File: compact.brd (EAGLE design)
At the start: 21.6 x 57.1 mm, 39 parts, among them J3 AVX_6-PIN_009159006061916, J4 CORTEX_DEBUG_PTH, J5 2172034-1, U1 STM32F103C8T6, U2 CJT1117-3.3-SOT223

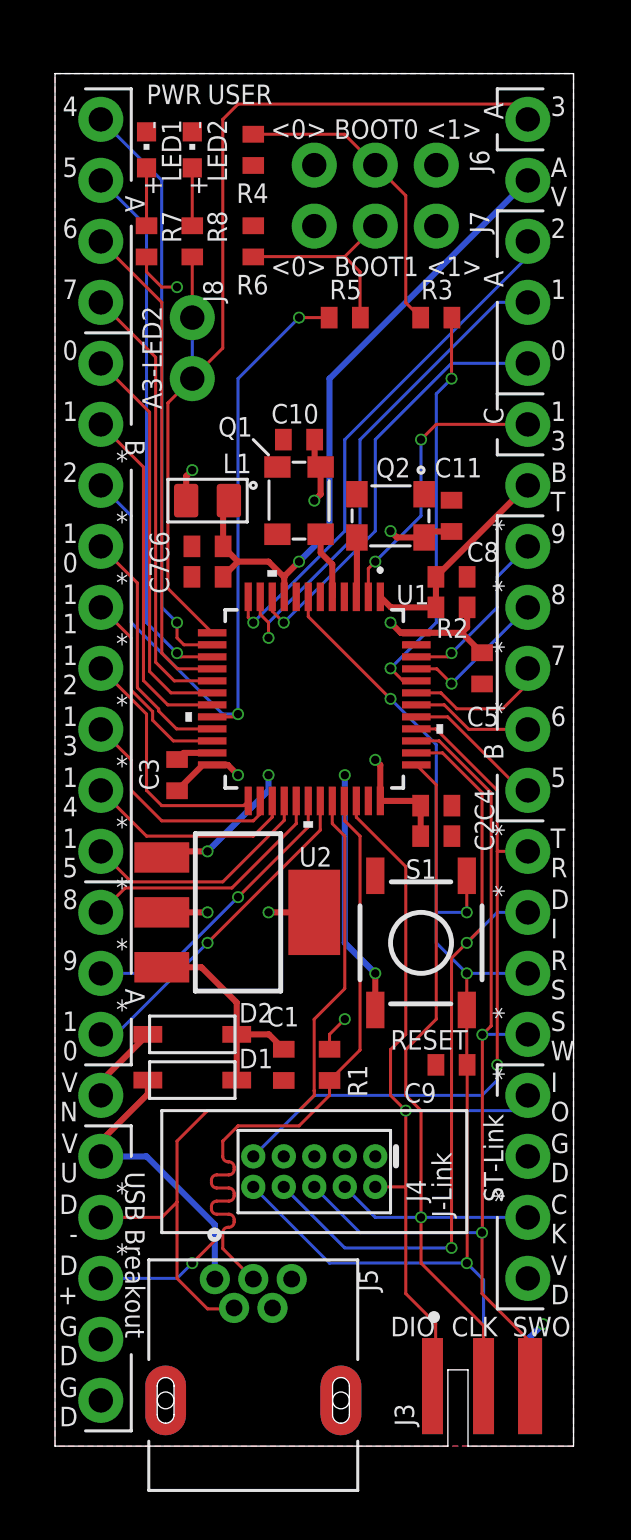
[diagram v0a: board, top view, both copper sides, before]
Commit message: Separated Standard configuration into Standard-no-HSE and Standard-with-HSE configurations.
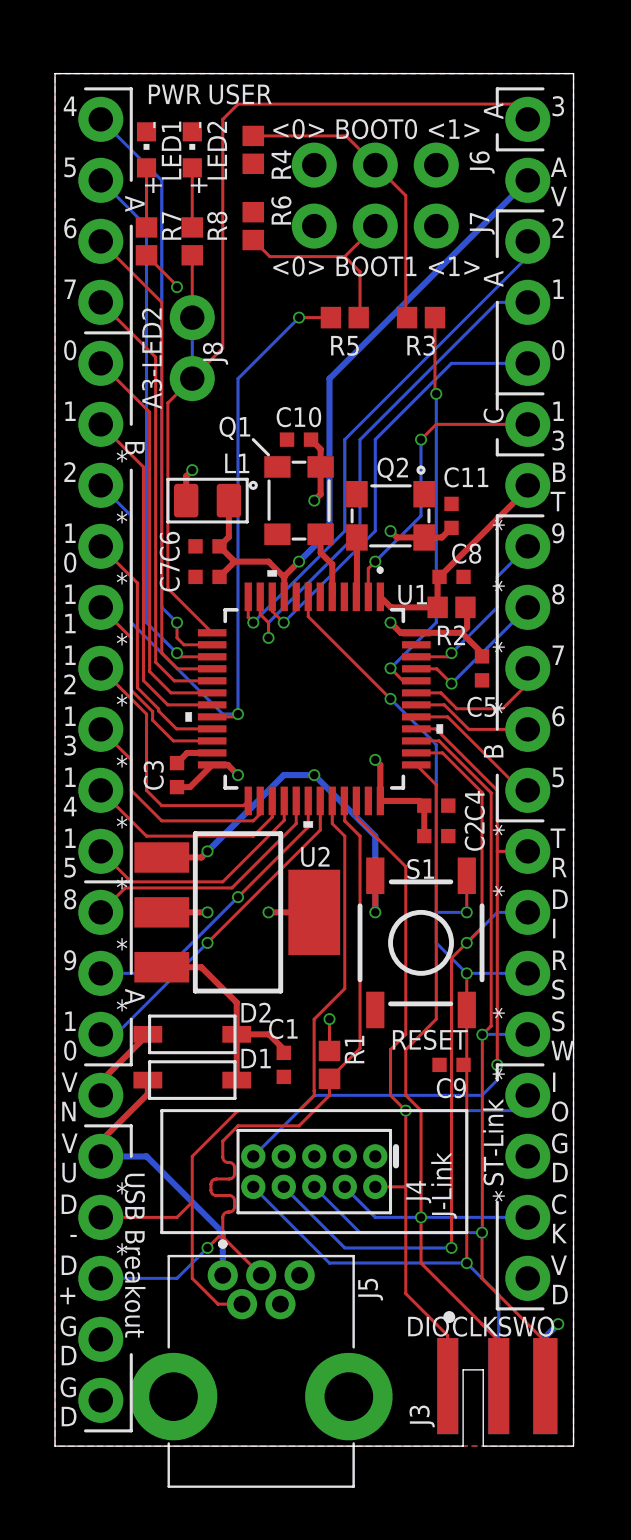
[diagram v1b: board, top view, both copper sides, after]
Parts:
- C1, C10, C11, C2, C3, C4, C5, C6, C7, C8, C9: device adafruit:C0402 -> SparkFun-Capacitors:0402-TIGHT
- J5: device USB-mini-B_TE_2172034-1:TE_2172034-1 -> 2172034-1:21720341
- R1, R2, R3, R4, R5, R6, R7, R8: device adafruit:R0402 -> SparkFun-Resistors:0402
- moved J5 5.36 mm to (6.99, 7.11)
- moved R3 0.63 mm to (15.2, 47.0)
- moved J3 0.63 mm to (18.4, 0.00)
- moved R6 0.63 mm to (8.26, 50.8)
- turned R8 to 270 degrees
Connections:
- net GND: now also J5.MH1, J5.MH2; no longer J5.SH1, J5.SH2
- net N$4: now also R8.1; no longer R8.2
- net PA3: now also R8.2; no longer R8.1
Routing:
- net USB_DP*: track 33.6 -> 32.3 mm
- net USB_DM*: track 31.6 -> 30.8 mm
- net GND: track 20.9 -> 20.5 mm, vias 5 -> 4
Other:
- outline, holes or cut-outs redrawn
- board text added: "-------POWER------- VDD/AVDD: 2-3.6V. Must be 3.3V if C39- 097/C387- 415 are used for Q1/Q2. VUSB: 5V from USB (J5) VIN: 4.8-15V BAT: 1.8-3.6V. Short R2 if unused. ***WARNING***: Do NOT power MCU from VDD if EITHER VIN or USB (J5) are also being used. --------GPIO-------- Max current, ea pin: 25 mA Max current, total: 150 mA OUT (minus MCU power, ~7 -50 mA) and 150 mA IN (minus MCU power) *=5V to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"
- board text added: "GD"
- board text removed: "-------POWER------- VDD/AVDD: 2-3.6V. Must be 3.3V if C39- 097/C387- 415 are used for Q1/Q2. VUSB: 5V from USB (J5) VIN: 4.8-15V BAT: 1.8-3.6V. Short R2 if unused. ***WARNING***: Do NOT power MCU from VDD if EITHER VIN or USB (J5) are also being used. --------GPIO-------- Max current, ea pin: 25 mA Max current, total: 150 mA OUT (minus MCU power, ~7 -50 mA) and 150 mA IN (minus MCU po- wer) *=5V 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"
- board text removed: "GND"

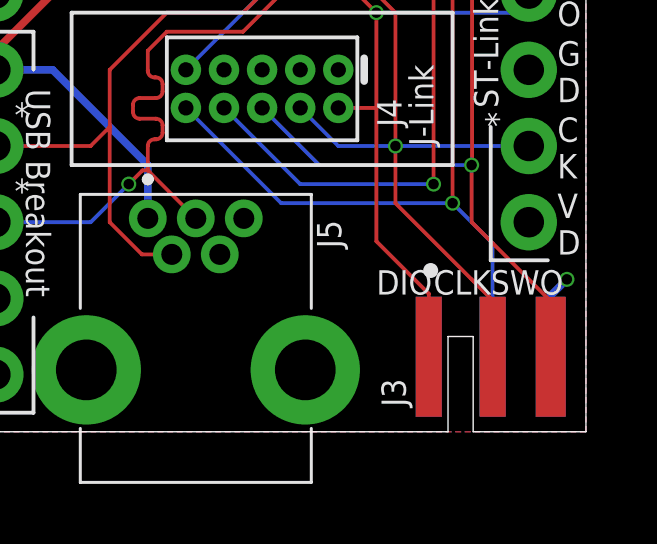
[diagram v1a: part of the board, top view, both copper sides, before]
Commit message: Updated Debug Edge library. Updated Gerbers, screenshots, and schematic image. Switched to new Mini-B USB footprint.
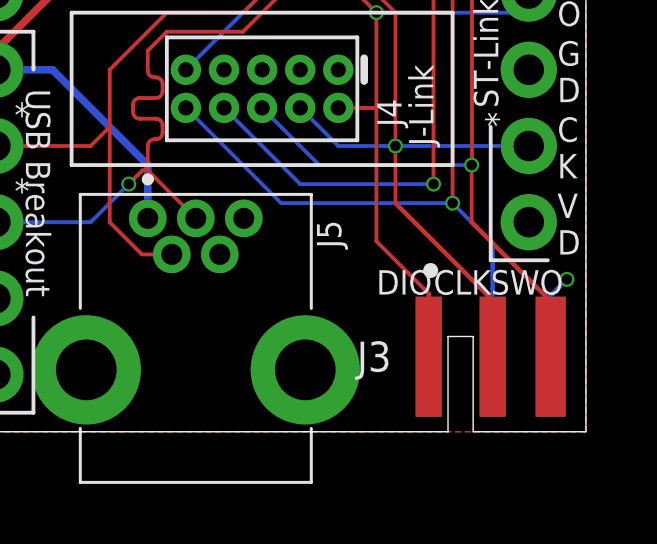
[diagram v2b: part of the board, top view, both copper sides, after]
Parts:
- J3: value AVX_6-PIN_009159006061916 -> AVX_6-PIN_009159006061916_33MIL-GAP; device Debug-Edge_AVX-connectors:AVX_6-PIN_009159006061916_0 -> Debug-Edge_AVX-connectors:AVX_6-PIN_009159006061916_33MIL-GAP
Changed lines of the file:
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@@
 <attribute name="VALUE" x="7.747" y="43.18" size="0.6096" layer="27" font="vector" ratio="20" rot="R90"/>
-</element>
-<element name="J3" library="Debug-Edge_AVX-connectors" package="AVX_6-PIN_009159006061916_0" value="AVX_6-PIN_009159006061916" x="18.415" y="0" smashed="yes">
-<attribute name="NAME" x="14.775" y="1.77" size="0.8128" layer="25" ratio="6" rot="R270"/>
 </element>
 <element name="L1" library="OPL_Ferrite_and_Magnetic_Bead" package="L0805" package3d_urn="urn:adsk.eagle:package:8004624/1" value="470R-2A" x="6.35" y="39.37" smashed="yes" rot="R180">
@@
 <attribute name="VALUE" x="8.585" y="3.412" size="1.27" layer="27" rot="R270" align="center"/>
 </element>
+<element name="J3" library="Debug-Edge_AVX-connectors" package="AVX_6-PIN_009159006061916_33MIL-GAP" value="AVX_6-PIN_009159006061916_33MIL-GAP" x="18.415" y="0" smashed="yes">
+<attribute name="NAME" x="15.105" y="3.005" size="1" layer="25" rot="R180"/>
+</element>
 </elements>
 <signals>
@@
 <contactref element="U1" pad="7"/>
 <contactref element="J4" pad="10"/>
-<contactref element="J3" pad="5"/>
 <contactref element="J2" pad="15"/>
 <wire x1="17.145" y1="18.161" x2="17.145" y2="19.685" width="0.127" layer="1"/>
@@
 <via x="17.145" y="22.225" extent="1-16" drill="0.35"/>
 <wire x1="17.145" y1="22.225" x2="15.875" y2="22.225" width="0.127" layer="16"/>
-<wire x1="17.145" y1="7.62" x2="17.78" y2="6.985" width="0.127" layer="16"/>
 <contactref element="C9" pad="1"/>
-<wire x1="17.78" y1="6.985" x2="17.8435" y2="6.9215" width="0.127" layer="16"/>
 <wire x1="17.145" y1="18.161" x2="17.145" y2="16.01" width="0.127" layer="1"/>
 <wire x1="17.145" y1="16.01" x2="17.01" y2="15.875" width="0.127" layer="1"/>
 <wire x1="17.01" y1="15.875" x2="17.145" y2="15.74" width="0.127" layer="1"/>
 <wire x1="17.145" y1="15.74" x2="17.145" y2="7.62" width="0.127" layer="1"/>
-<wire x1="17.8435" y1="6.9215" x2="18.4785" y2="6.2865" width="0.127" layer="16"/>
-<wire x1="18.4785" y1="6.2865" x2="18.4785" y2="2.5" width="0.127" layer="16"/>
+<wire x1="17.145" y1="7.62" x2="18.415" y2="6.35" width="0.127" layer="16"/>
+<contactref element="J3" pad="5"/>
+<wire x1="18.415" y1="6.35" x2="18.4785" y2="6.2865" width="0.1524" layer="16"/>
+<wire x1="18.4785" y1="6.2865" x2="18.4785" y2="2.5" width="0.1524" layer="16"/>
 </signal>
 <signal name="BOOT0">
@@
 <wire x1="15.045" y1="33.865" x2="16.935" y2="33.865" width="0.254" layer="1"/>
 <wire x1="17.16" y1="34.09" x2="16.935" y2="33.865" width="0.254" layer="1"/>
-<contactref element="J3" pad="4"/>
 <contactref element="L1" pad="2"/>
 <contactref element="J2" pad="20"/>
@@
 <wire x1="17.78" y1="33.02" x2="17.78" y2="32.885" width="0.254" layer="1"/>
 <wire x1="16.935" y1="33.865" x2="17.78" y2="33.02" width="0.254" layer="1"/>
+<contactref element="J3" pad="4"/>
 </signal>
 <signal name="GND">
@@
 <contactref element="J6" pad="1"/>
 <contactref element="J7" pad="1"/>
-<contactref element="J3" pad="6"/>
 <contactref element="J2" pad="18"/>
 <contactref element="J9" pad="10"/>
@@
 <contactref element="J5" pad="MH2"/>
 <contactref element="J5" pad="MH1"/>
-<wire x1="20.415" y1="2.5" x2="20.415" y2="4.54" width="0.254" layer="16"/>
-<wire x1="20.415" y1="4.54" x2="20.955" y2="5.08" width="0.254" layer="16"/>
+<contactref element="J3" pad="6"/>
+<wire x1="20.415" y1="2.5" x2="20.415" y2="4.54" width="0.1524" layer="16"/>
+<wire x1="20.415" y1="4.54" x2="20.955" y2="5.08" width="0.1524" layer="16"/>
 <via x="20.955" y="5.08" extent="1-16" drill="0.35"/>
 </signal>
@@
 <contactref element="U1" pad="34"/>
 <contactref element="J4" pad="2"/>
-<contactref element="J3" pad="1"/>
 <contactref element="J2" pad="17"/>
 <wire x1="12.545" y1="26.865" x2="12.545" y2="26.19" width="0.127" layer="1"/>
@@
 <wire x1="14.605" y1="10.795" x2="14.605" y2="6.35" width="0.127" layer="1"/>
 <wire x1="13.335" y1="10.795" x2="14.605" y2="10.795" width="0.127" layer="1"/>
-<wire x1="16.3515" y1="4.6035" x2="16.3515" y2="2.5" width="0.127" layer="1"/>
 <wire x1="14.605" y1="6.35" x2="16.3515" y2="4.6035" width="0.127" layer="1"/>
+<contactref element="J3" pad="1"/>
+<wire x1="16.3515" y1="4.6035" x2="16.3515" y2="2.5" width="0.1524" layer="1"/>
 </signal>
 <signal name="SWCLK*">
 <contactref element="U1" pad="37"/>
 <contactref element="J4" pad="4"/>
-<contactref element="J3" pad="2"/>
 <contactref element="J2" pad="19"/>
 <wire x1="15.045" y1="28.365" x2="15.875" y2="27.535" width="0.127" layer="1"/>
@@
 <wire x1="13.335" y1="9.525" x2="12.065" y2="10.795" width="0.127" layer="16"/>
 <wire x1="15.24" y1="9.525" x2="15.24" y2="7.62" width="0.127" layer="1"/>
-<wire x1="15.24" y1="7.62" x2="17.78" y2="5.08" width="0.127" layer="1"/>
-<wire x1="17.78" y1="5.08" x2="17.8435" y2="5.0165" width="0.127" layer="1"/>
-<wire x1="17.8435" y1="5.0165" x2="18.4785" y2="4.3815" width="0.127" layer="1"/>
-<wire x1="18.4785" y1="4.3815" x2="18.4785" y2="2.5" width="0.127" layer="1"/>
+<contactref element="J3" pad="2"/>
+<wire x1="18.4785" y1="4.3815" x2="18.4785" y2="2.5" width="0.1524" layer="1"/>
+<wire x1="15.24" y1="7.62" x2="18.4785" y2="4.3815" width="0.1524" layer="1"/>
 </signal>
 <signal name="PB6*">
@@
 <contactref element="U1" pad="39"/>
 <contactref element="J4" pad="6"/>
-<contactref element="J3" pad="3"/>
 <contactref element="J2" pad="16"/>
 <wire x1="15.045" y1="29.365" x2="15.9957875" y2="29.365" width="0.127" layer="1"/>
@@
 <wire x1="12.7" y1="8.89" x2="10.795" y2="10.795" width="0.127" layer="16"/>
 <wire x1="17.78" y1="8.89" x2="17.78" y2="6.985" width="0.127" layer="1"/>
-<wire x1="20.415" y1="4.35" x2="20.415" y2="2.5" width="0.127" layer="1"/>
-<wire x1="17.78" y1="6.985" x2="20.415" y2="4.35" width="0.127" layer="1"/>
+<contactref element="J3" pad="3"/>
+<wire x1="20.415" y1="4.35" x2="20.415" y2="2.5" width="0.1524" layer="1"/>
+<wire x1="17.78" y1="6.985" x2="20.415" y2="4.35" width="0.1524" layer="1"/>
 </signal>
 <signal name="PB8*">
